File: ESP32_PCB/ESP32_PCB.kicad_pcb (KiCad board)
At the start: 2 copper layers, 35 x 35 mm, 35 parts, among them J1 USB_C_Receptacle, J2 ESC 1, J3 ESC 2, J4 EN & Boot, J5 LED, U2 H3LIS331DL, U3 AP2112K-3.3, U4 TPS54302, U5 ESP32-S3-MINI-1U

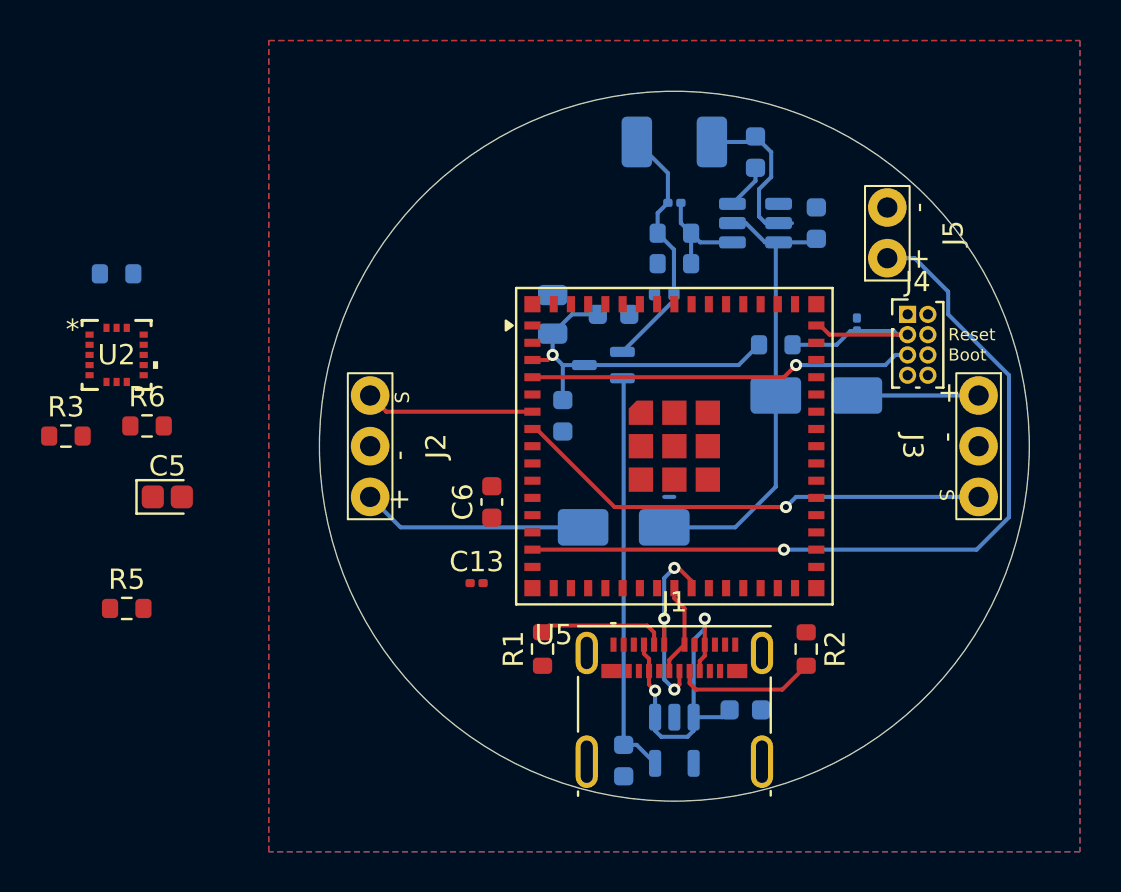
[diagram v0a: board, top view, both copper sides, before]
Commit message: Add tracks for gyro
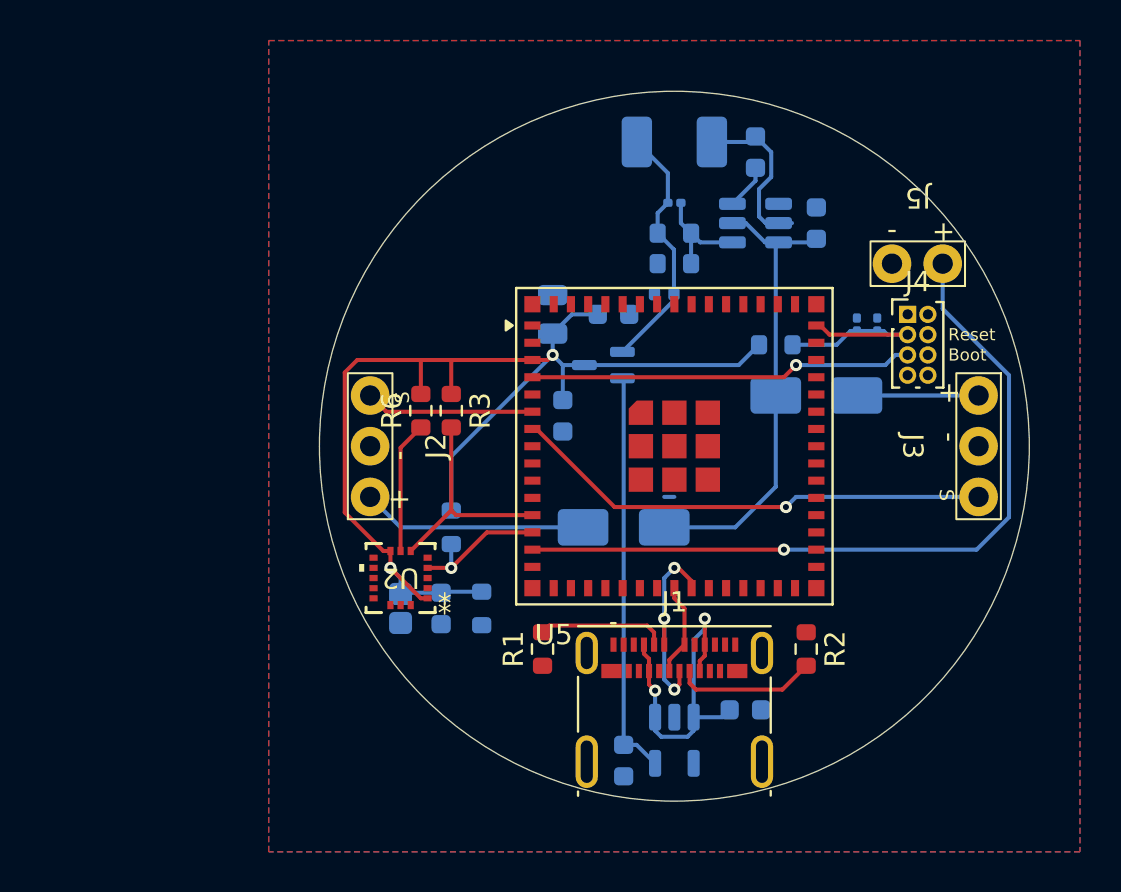
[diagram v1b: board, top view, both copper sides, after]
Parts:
- C13, C5, C6, R5: moved to B.Cu
- moved C13 23.5 mm to (160.0, 94.0), turned to -90 degrees
- moved R4 20.7 mm to (139.0, 104.0), turned to -90 degrees
- moved R3 19.0 mm to (139.0, 98.2), turned to -90 degrees
- moved U2 17.8 mm to (136.5, 106.5), turned to 180 degrees
- moved R5 17.5 mm to (140.5, 108.0), turned to 90 degrees
- moved R6 13.5 mm to (137.5, 98.2), turned to 90 degrees
- moved C5 12.7 mm to (136.5, 108.0), turned to -90 degrees
- moved C6 5.81 mm to (138.5, 108.0), turned to -90 degrees
- moved J5 2.12 mm to (162.0, 91.0), turned to 180 degrees
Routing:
- net +3V3: track 17.3 -> 58.7 mm, vias 1 -> 2
- net /SDA: track 0.00 -> 11.0 mm
- net /SCL: track 0.00 -> 7.07 mm, vias 0 -> 1
- net /SA0: track 0.00 -> 6.51 mm
- net /LED: track 40.2 -> 38.0 mm

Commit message: Place thermal pad vias
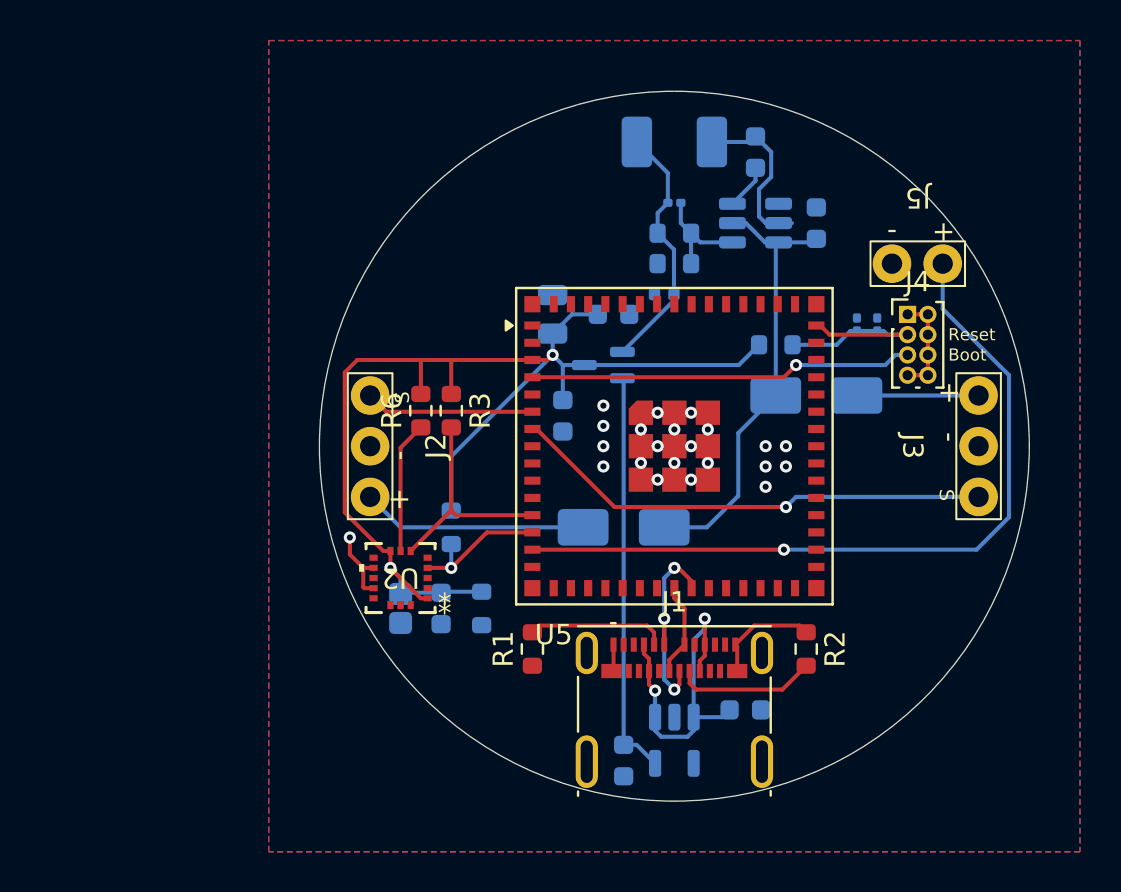
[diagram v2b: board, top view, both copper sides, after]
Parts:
- moved R1 0.50 mm to (143.0, 110.0)
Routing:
- net GNDREF: track 0.00 -> 15.5 mm, vias 0 -> 22
- net VBATT: track 23.5 -> 22.2 mm
- net Net-(J1-CC1): track 6.38 -> 6.88 mm

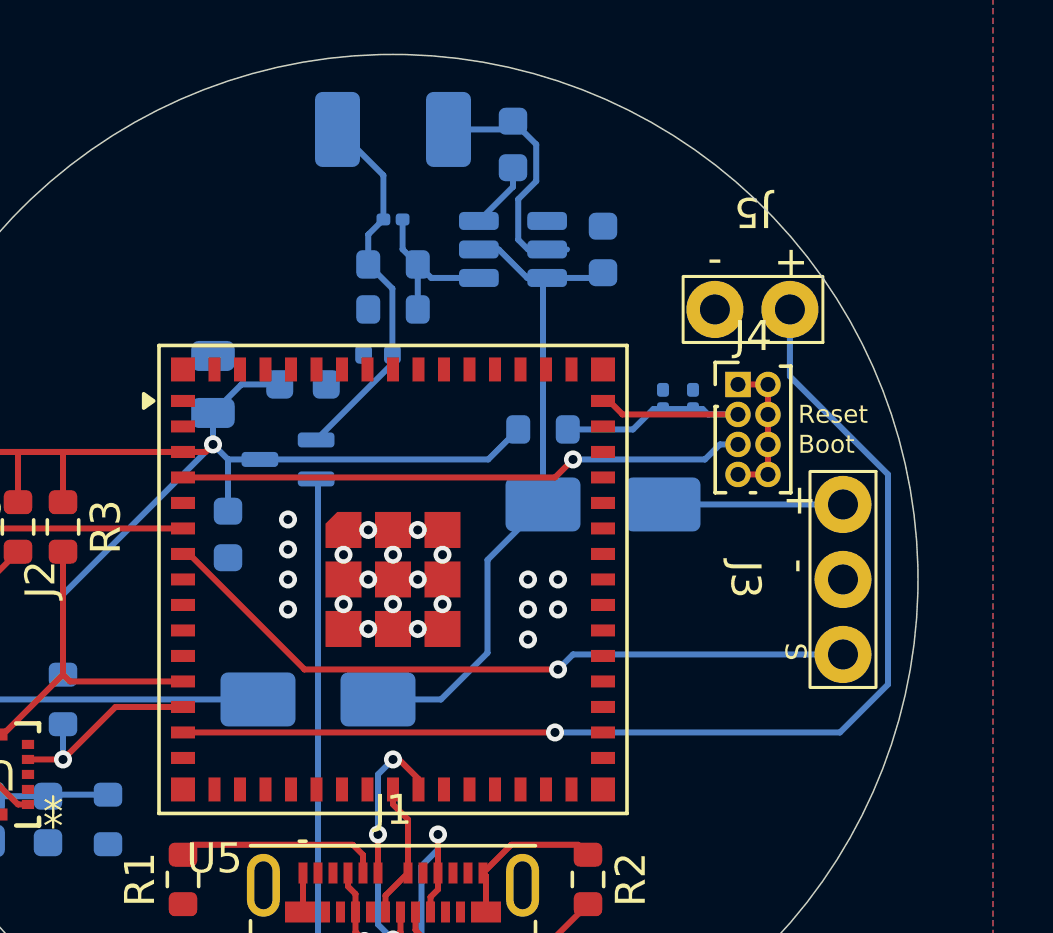
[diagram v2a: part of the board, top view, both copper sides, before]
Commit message: Fix the size of the header pins
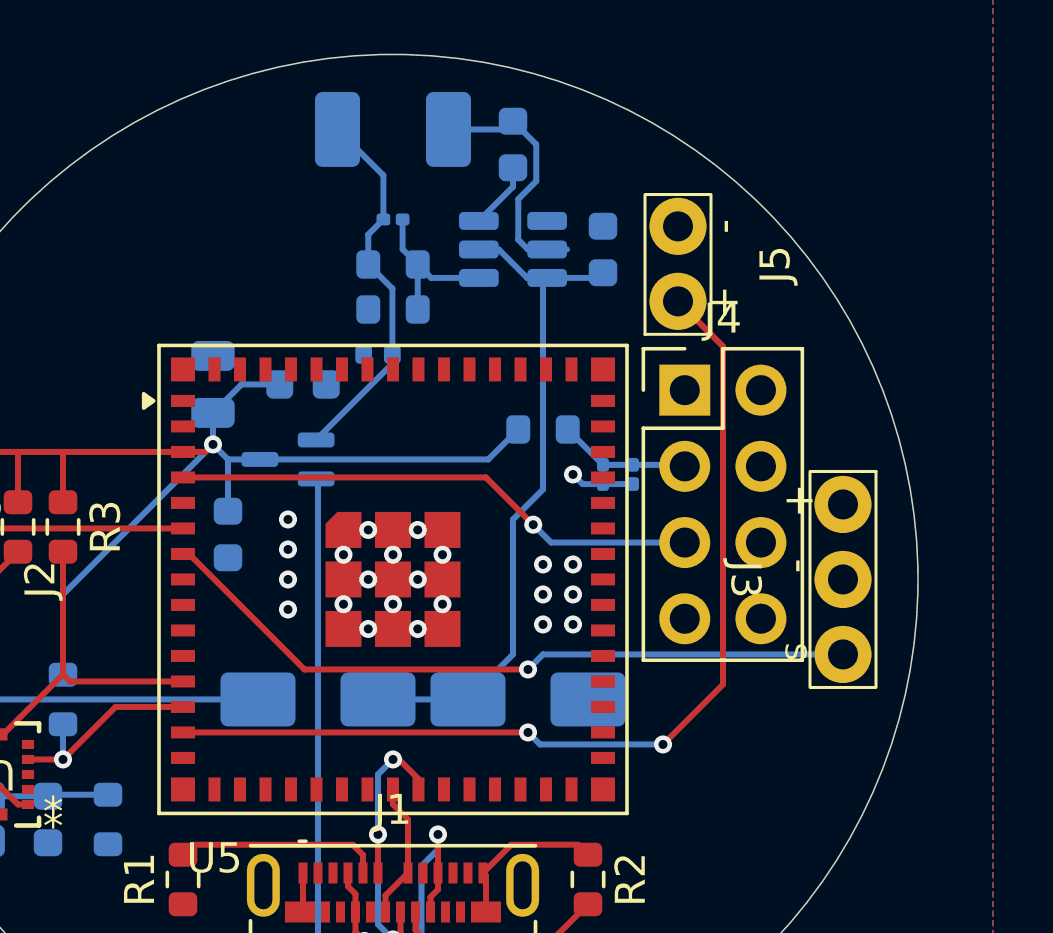
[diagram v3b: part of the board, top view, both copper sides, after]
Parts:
- J4: footprint Connector_PinHeader_1.00mm:PinHeader_2x04_P1.00mm_Vertical -> Connector_PinHeader_2.54mm:PinHeader_2x04_P2.54mm_Vertical
- moved D3 6.96 mm to (154.5, 104.0)
- moved C13 3.91 mm to (157.0, 96.5), turned to 90 degrees
- moved J5 2.92 mm to (159.5, 89.5), turned to 90 degrees
- moved C12 2.69 mm to (158.0, 96.5), turned to 90 degrees
- moved J4 1.79 mm to (159.7, 93.7)
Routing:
- net /EN: track 10.7 -> 4.41 mm
- net Net-(D3-A2): track 6.00 -> 0.00 mm
- net /LED: track 38.0 -> 32.4 mm, vias 1 -> 2
- net GNDREF: track 15.5 -> 12.6 mm, vias 22 -> 24
- net /BOOT: track 19.0 -> 17.6 mm
- net VBATT: track 22.2 -> 22.7 mm
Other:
- board text removed: "Boot"
- board text removed: "Reset"

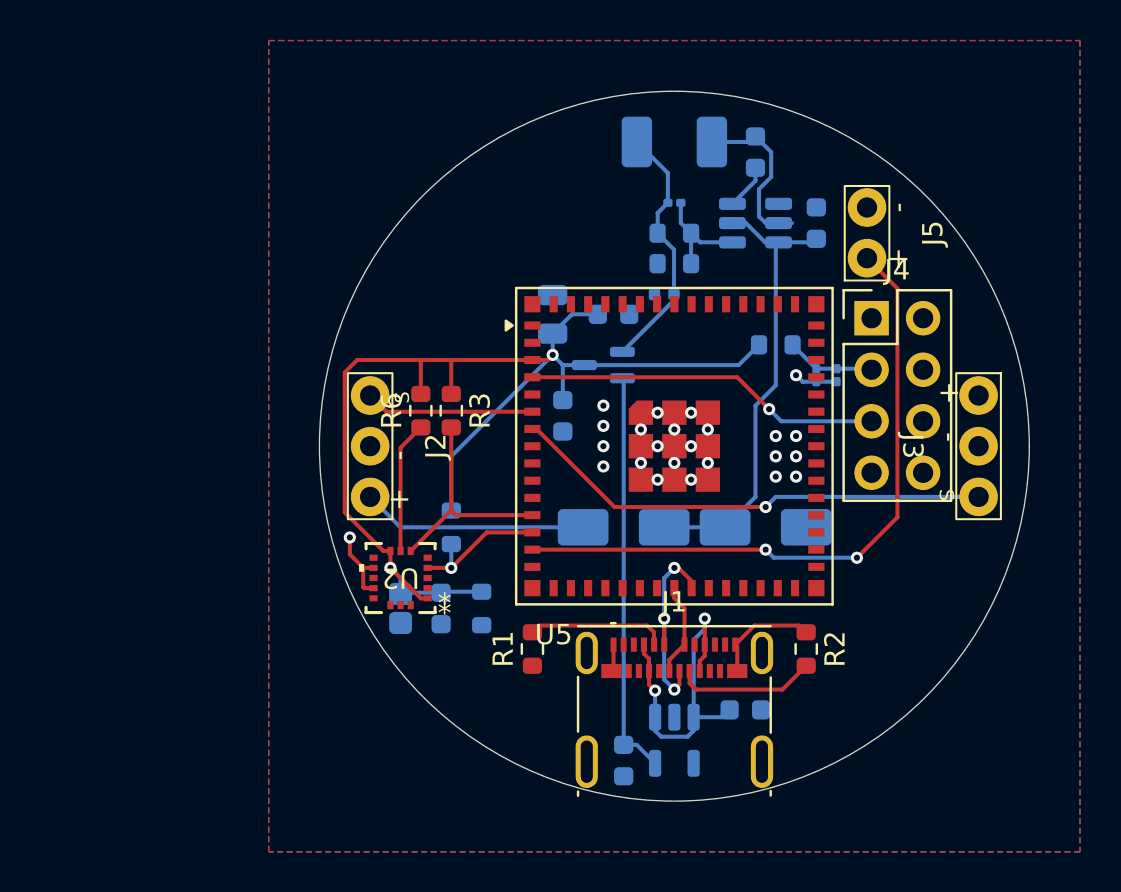
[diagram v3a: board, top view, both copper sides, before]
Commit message: Add labels on PCB
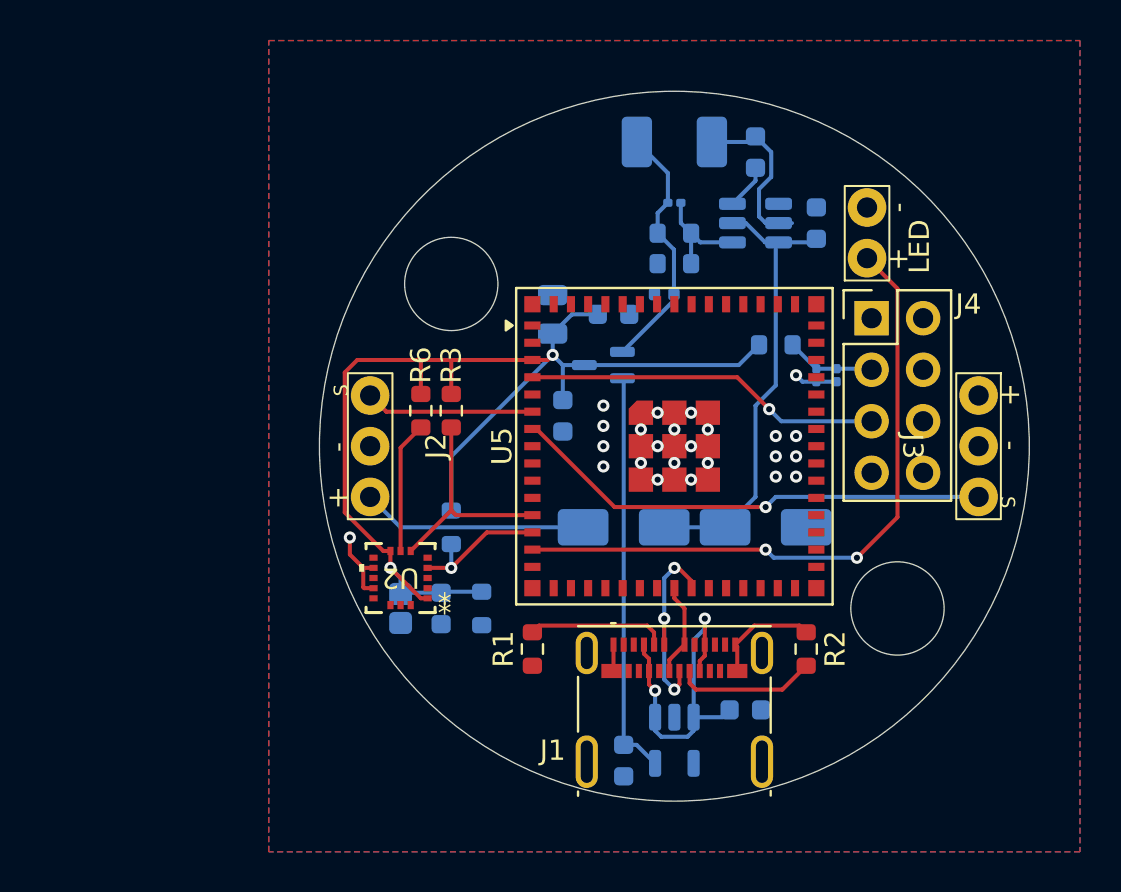
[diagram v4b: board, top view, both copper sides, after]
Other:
- outline, holes or cut-outs redrawn
- board text added: "*"
- board text added: "Boot"
- board text added: "LED"
- board text added: "Reset"

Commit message: Add screw holes and Stuffed Crust logo
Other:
- board text added: "M2 Screw"
- board text added: "Stuffed Crust"
- board text added: "Wildcat Robotics"
